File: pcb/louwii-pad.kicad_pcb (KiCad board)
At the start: 2 copper layers, 88 x 106 mm, 37 parts, among them J1 USB_B_Micro, J2 ICSP, J3 IIC, K1 KEYSW, K2 KEYSW, K3 KEYSW, K4 KEYSW, K5 KEYSW, K6 KEYSW, K7 KEYSW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

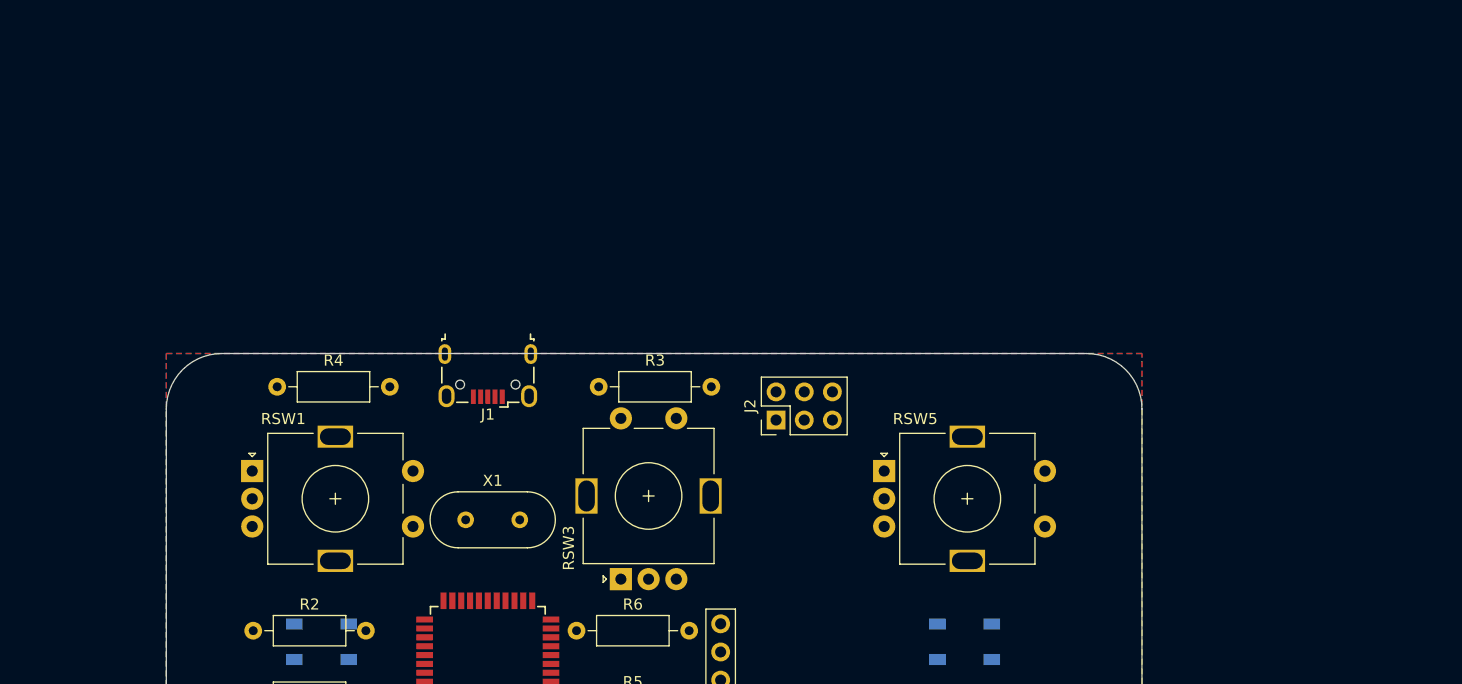
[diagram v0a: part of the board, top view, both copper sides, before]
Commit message: update schematics, update net, update footprints, update pcb design with missing footprints
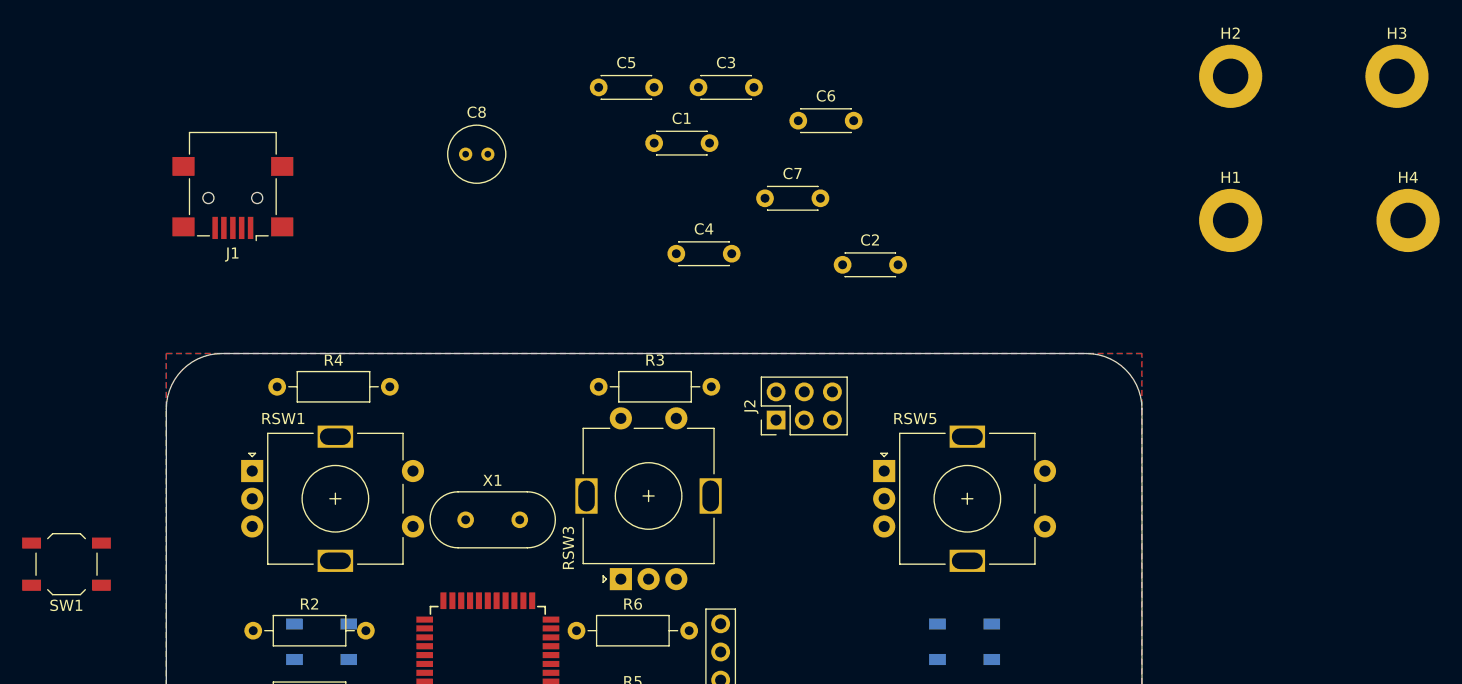
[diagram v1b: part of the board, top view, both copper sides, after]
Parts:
- added C1: 22pF, Capacitor_THT:C_Disc_D4.3mm_W1.9mm_P5.00mm, F.Cu at (105.0, 61.0)
- added C2: 22pF, Capacitor_THT:C_Disc_D4.3mm_W1.9mm_P5.00mm, F.Cu at (122.0, 72.0)
- added C3: 1uF, Capacitor_THT:C_Disc_D4.3mm_W1.9mm_P5.00mm, F.Cu at (109.0, 56.0)
- added C4: 0.1uF, Capacitor_THT:C_Disc_D4.3mm_W1.9mm_P5.00mm, F.Cu at (107.0, 71.0)
- added C5: 0.1uF, Capacitor_THT:C_Disc_D4.3mm_W1.9mm_P5.00mm, F.Cu at (100.0, 56.0)
- added C6: 0.1uF, Capacitor_THT:C_Disc_D4.3mm_W1.9mm_P5.00mm, F.Cu at (118.0, 59.0)
- added C7: 0.1uF, Capacitor_THT:C_Disc_D4.3mm_W1.9mm_P5.00mm, F.Cu at (115.0, 66.0)
- added C8: 4.7uF, Capacitor_THT:C_Radial_D5.0mm_H7.0mm_P2.00mm, F.Cu at (88.0, 62.0)
- added H1: MountingHole 3mm, MountingHole:MountingHole_3.2mm_M3_ISO7380_Pad, F.Cu at (157.0, 68.0)
- added H2: MountingHole 3mm, MountingHole:MountingHole_3.2mm_M3_ISO7380_Pad, F.Cu at (157.0, 55.0)
- added H3: MountingHole 3mm, MountingHole:MountingHole_3.2mm_M3_ISO7380_Pad, F.Cu at (172.0, 55.0)
- added H4: MountingHole 3mm, MountingHole:MountingHole_3.2mm_M3_ISO7380_Pad, F.Cu at (173.0, 68.0)
- added SW1: SW_Push, Button_Switch_SMD:SW_SPST_TL3342, F.Cu at (52.0, 99.0)
- J1: value USB_B_Micro -> USB_B_Mini; footprint Connector_USB:USB_Micro-B_Wuerth_629105150521 -> Connector_USB:USB_Mini-B_Lumberg_2486_01_Horizontal
- X1: value Crystal -> 16Mhz
- moved J1 28.0 mm to (67.0, 66.0)
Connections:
- J1 pad 4: Net-(J1-Pad4) -> (no net)
- RGB4 pad 2: Net-(RGB4-Pad2) -> (no net)
- RSW2 pad S1: Net-(RSW2-PadS1) -> (no net)
- RSW2 pad S2: Net-(RSW2-PadS2) -> (no net)
- RSW3 pad S1: Net-(RSW3-PadS1) -> (no net)
- RSW3 pad S2: Net-(RSW3-PadS2) -> (no net)
- RSW4 pad S1: Net-(RSW4-PadS1) -> (no net)
- RSW4 pad S2: Net-(RSW4-PadS2) -> (no net)
- RSW5 pad S1: Net-(RSW5-PadS1) -> (no net)
- RSW5 pad S2: Net-(RSW5-PadS2) -> (no net)
- RSW6 pad S1: Net-(RSW6-PadS1) -> (no net)
- RSW6 pad S2: Net-(RSW6-PadS2) -> (no net)
- U1 pad 42: Net-(U1-Pad42) -> (no net)

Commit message: add more 3d models, finish up PCB tracing
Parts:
- C1, C2, C4, C5, C6, D1, D2, D3, D4, R2: moved to B.Cu
- moved H3 164.7 mm to (66.0, 181.0)
- moved H4 116.7 mm to (144.0, 181.0)
- moved H1 92.6 mm to (66.0, 85.0)
- moved SW1 73.1 mm to (124.5, 108.1), turned to 0 degrees
- moved C5 65.3 mm to (93.3, 121.0), turned to 270 degrees
- moved C6 60.9 mm to (77.0, 104.0), turned to 180 degrees
- moved C8 56.6 mm to (114.1, 112.3)
- moved J1 54.4 mm to (118.0, 85.0)
- moved R4 54.0 mm to (122.0, 100.6), turned to 90 degrees
- moved C4 53.5 mm to (88.0, 121.0), turned to 270 degrees
- moved C3 52.3 mm to (104.5, 108.1)
- moved RGB3 49.8 mm to (124.0, 161.0)
- moved RGB2 49.0 mm to (124.0, 105.0), turned to 180 degrees
- moved RGB1 48.0 mm to (85.0, 105.0)
- moved RGB4 47.9 mm to (86.0, 161.0)
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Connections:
- U1 pad 1: RSW1_S1 -> RSW6_A
- U1 pad 12: RSW2_B -> RSW5_A
- U1 pad 20: RSW4_A -> RSW3_A
- U1 pad 21: RSW4_B -> RSW3_B
- U1 pad 22: RSW5_B -> RSW1_S1
- U1 pad 25: RSW5_A -> RSW1_B
- U1 pad 26: RSW6_A -> RSW1_A
- U1 pad 27: RSW6_B -> row0
- U1 pad 28: RSW1_B -> row1
- U1 pad 30: RSW2_A -> col0
- U1 pad 31: RSW3_A -> col1
- U1 pad 32: RSW3_B -> col2
- U1 pad 36: col0 -> RSW2_B
- U1 pad 37: col1 -> RSW2_A
- U1 pad 38: col2 -> col3
- U1 pad 39: col3 -> RSW4_B
- U1 pad 40: row1 -> RSW4_A
- U1 pad 41: row0 -> RSW6_B
- U1 pad 8: RSW1_A -> RSW5_B
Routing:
- net VCC: track 0.00 -> 537.2 mm, vias 0 -> 3
- net row1: track 0.00 -> 99.9 mm
- net row0: track 0.00 -> 97.0 mm
- net col2: track 0.00 -> 95.2 mm
- net col3: track 0.00 -> 92.8 mm
- net col1: track 0.00 -> 88.5 mm
- net Net-(RGB2-Pad2): track 0.00 -> 82.0 mm
- net RST: track 0.00 -> 72.7 mm, vias 0 -> 1
- net col0: track 0.00 -> 71.6 mm
- net SCL: track 0.00 -> 66.3 mm
- net MISO: track 0.00 -> 64.2 mm, vias 0 -> 2
- net SCK: track 0.00 -> 63.2 mm, vias 0 -> 2
- net MOSI: track 0.00 -> 57.6 mm, vias 0 -> 2
- net SDA: track 0.00 -> 49.5 mm
- net Net-(RGB1-Pad2): track 0.00 -> 48.4 mm
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
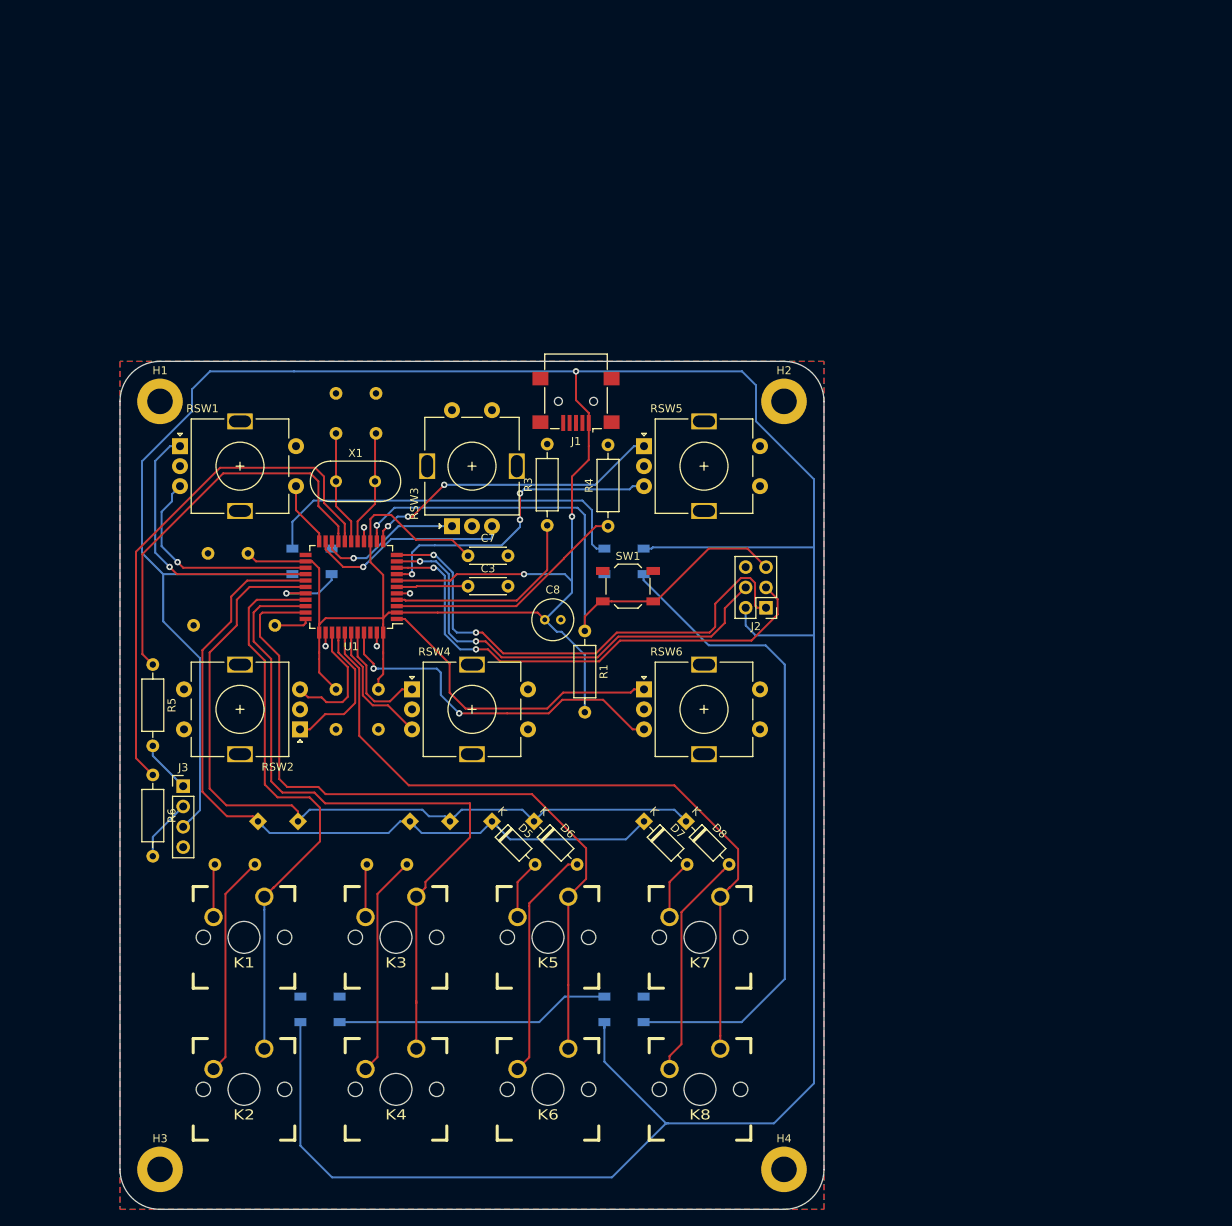
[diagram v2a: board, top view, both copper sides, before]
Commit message: finish up tracing, updating footprints, adding 3d models
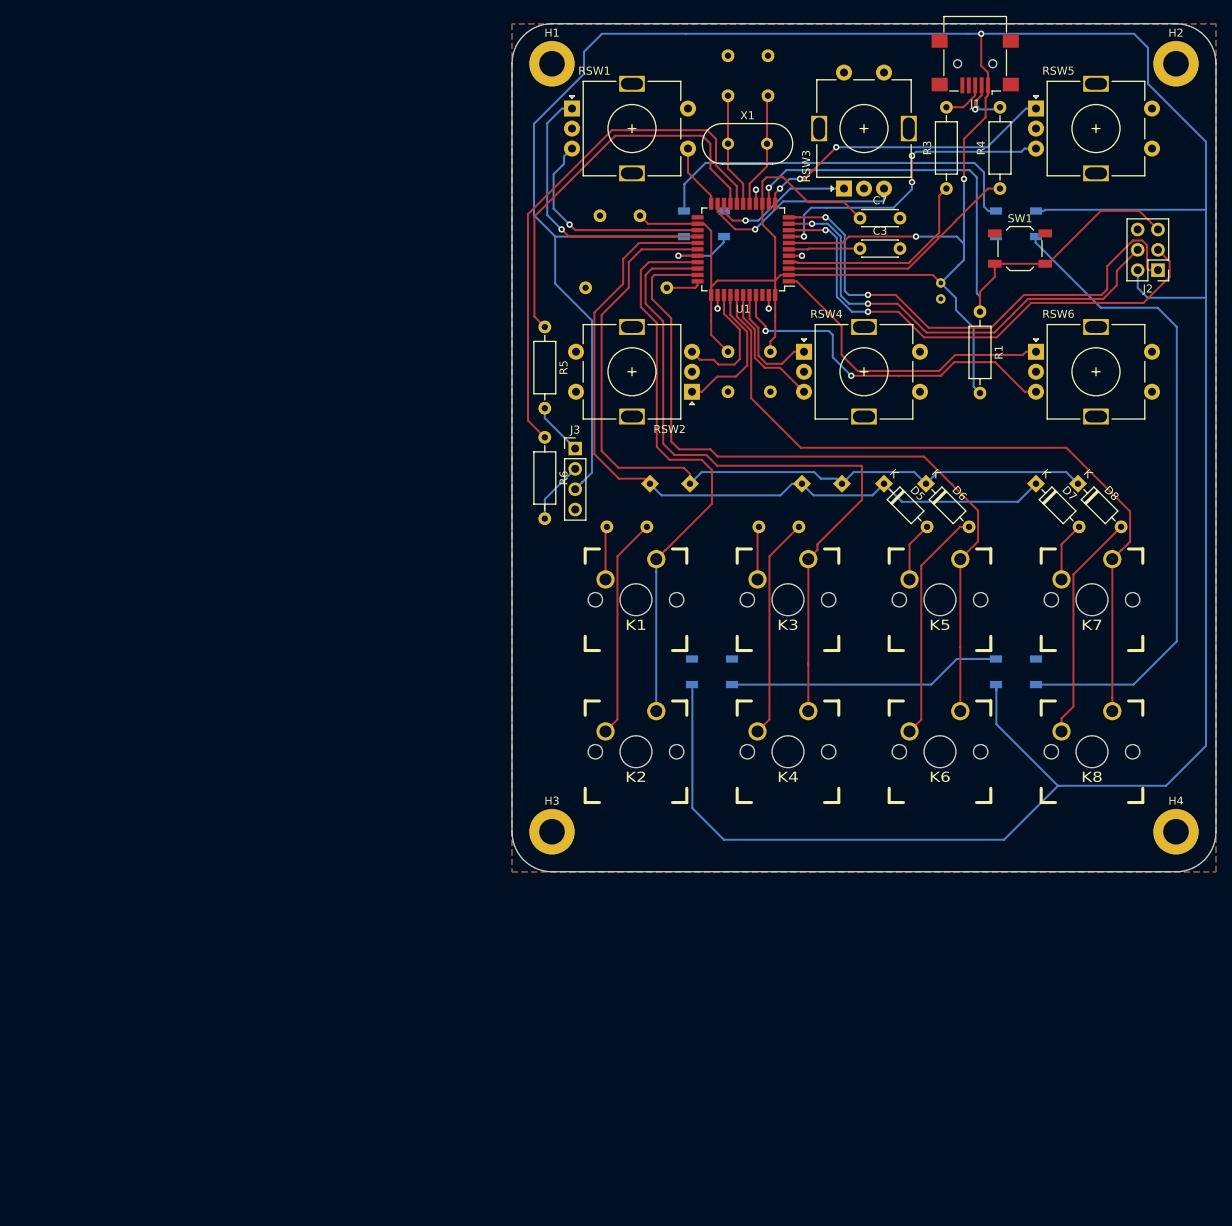
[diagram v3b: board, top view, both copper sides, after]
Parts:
- C8: moved to B.Cu
- RGB1, RGB2, RGB3, RGB4: footprint LED_SMD:LED_WS2812B_PLCC4_5.0x5.0mm_P3.2mm -> keyboard_parts:WS2812b
- moved J1 65.4 mm to (167.9, 42.8)
- moved R3 65.3 mm to (164.3, 58.4)
- moved C8 65.0 mm to (163.6, 70.2), turned to 270 degrees
- moved C5 64.7 mm to (142.3, 78.8)
- moved C1 64.7 mm to (137.0, 41.8)
- moved C2 64.7 mm to (142.0, 46.8)
- moved C4 64.7 mm to (137.0, 78.8)
- moved C6 64.7 mm to (126.0, 61.8)
- moved D1 64.7 mm to (127.2, 95.3)
- moved D2 64.7 mm to (132.2, 95.3)
- moved D3 64.7 mm to (146.2, 95.3)
- moved D4 64.7 mm to (151.2, 95.3)
- moved D5 64.7 mm to (156.5, 95.3)
- moved D6 64.7 mm to (161.8, 95.3)
- moved D7 64.7 mm to (175.5, 95.3)
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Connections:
- J1 pad 4: (no net) -> Net-(J1-Pad4)
- RGB4 pad 2: (no net) -> Net-(RGB4-Pad2)
- RSW2 pad S1: (no net) -> Net-(RSW2-PadS1)
- RSW2 pad S2: (no net) -> Net-(RSW2-PadS2)
- RSW3 pad S1: (no net) -> Net-(RSW3-PadS1)
- RSW3 pad S2: (no net) -> Net-(RSW3-PadS2)
- RSW4 pad S1: (no net) -> Net-(RSW4-PadS1)
- RSW4 pad S2: (no net) -> Net-(RSW4-PadS2)
- RSW5 pad S1: (no net) -> Net-(RSW5-PadS1)
- RSW5 pad S2: (no net) -> Net-(RSW5-PadS2)
- RSW6 pad S1: (no net) -> Net-(RSW6-PadS1)
- RSW6 pad S2: (no net) -> Net-(RSW6-PadS2)
- U1 pad 42: (no net) -> Net-(U1-Pad42)
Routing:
- net Net-(J1-Pad2): track 0.00 -> 6.54 mm, vias 0 -> 1
- net Net-(J1-Pad3): track 0.00 -> 5.47 mm
- net RST: track 72.7 -> 77.5 mm
- net VCC: track 537.2 -> 539.6 mm
- net SCK: track 63.2 -> 64.6 mm
- net MOSI: track 57.6 -> 58.9 mm
- net MISO: track 64.2 -> 65.5 mm

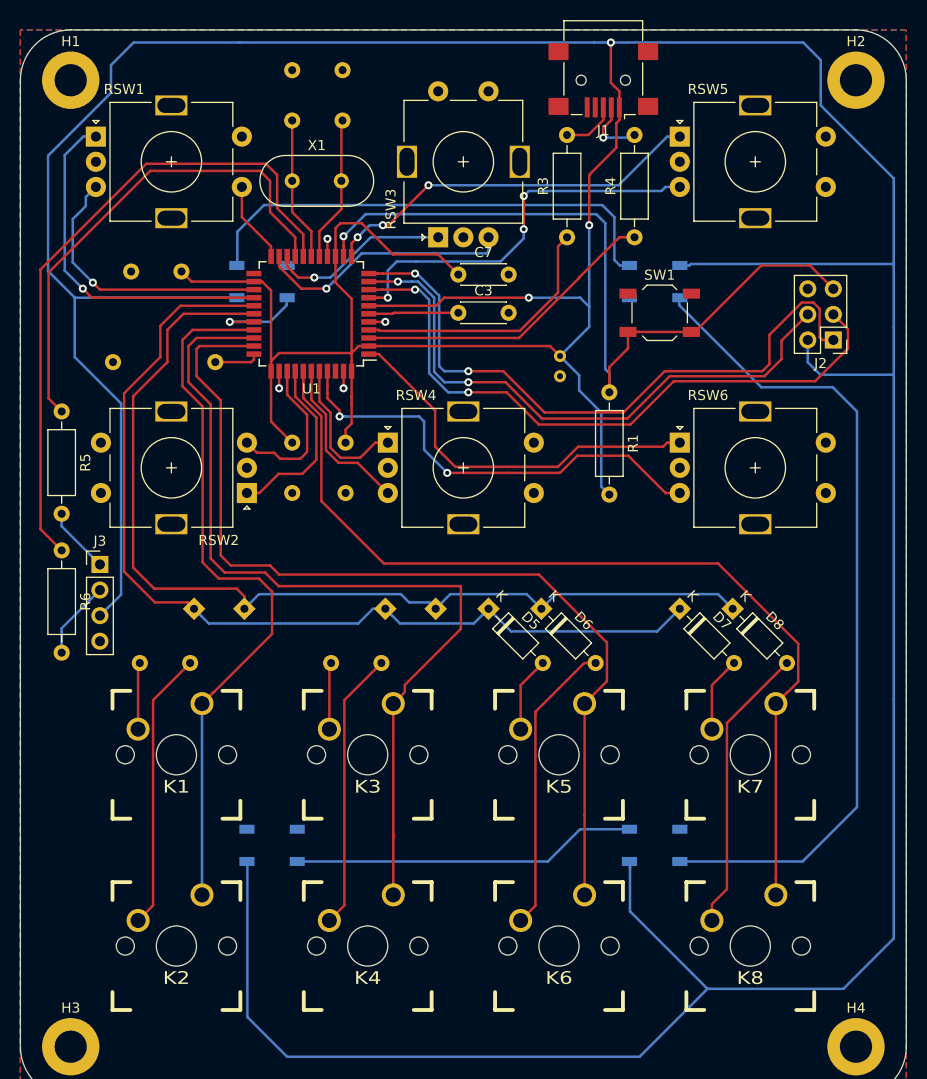
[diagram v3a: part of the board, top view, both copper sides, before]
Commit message: cleanup silk layers
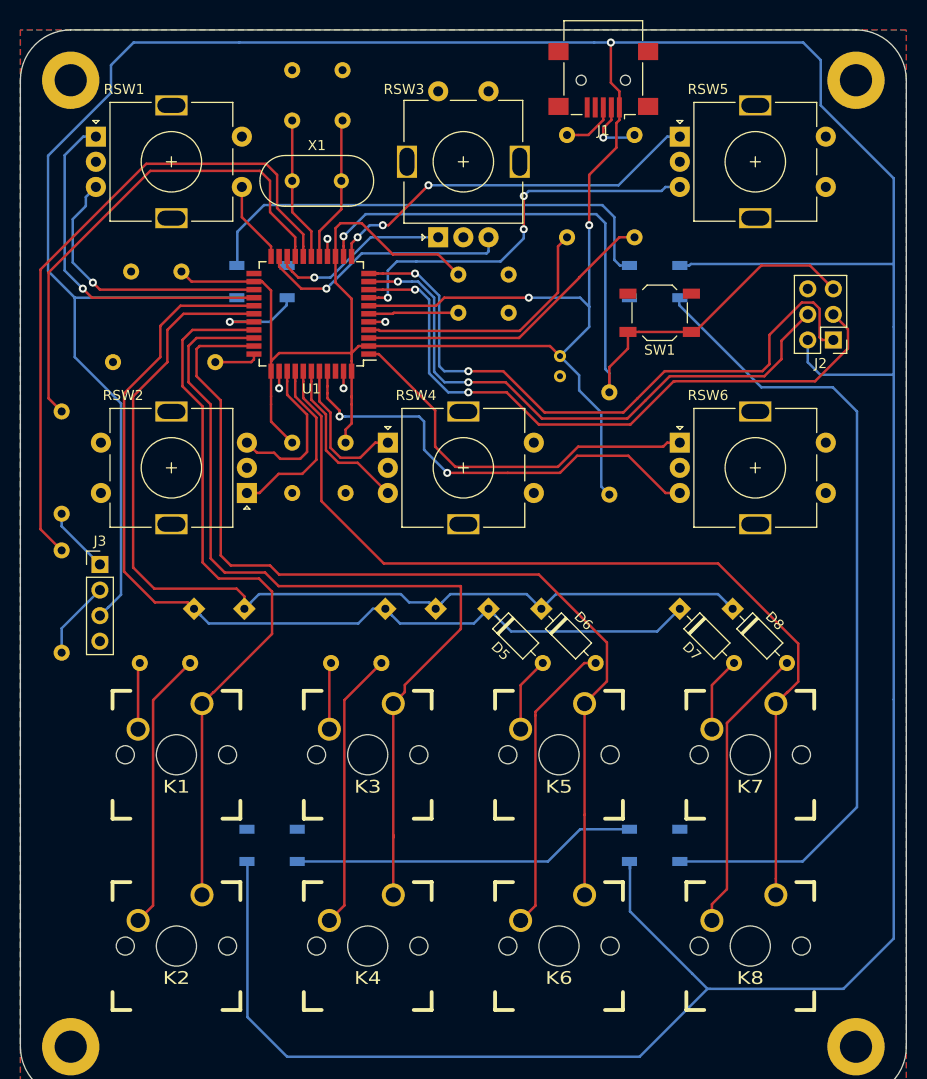
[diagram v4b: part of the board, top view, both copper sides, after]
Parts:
- C3, C7, R1, R3, R4, R5, R6: moved to B.Cu
- turned H1 to 180 degrees
- turned H2 to 180 degrees
